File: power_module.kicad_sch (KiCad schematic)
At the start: 3 parts, among them J2 OUTPUT, J3 I2C_BREAKOUT, SW1 ON_OFF

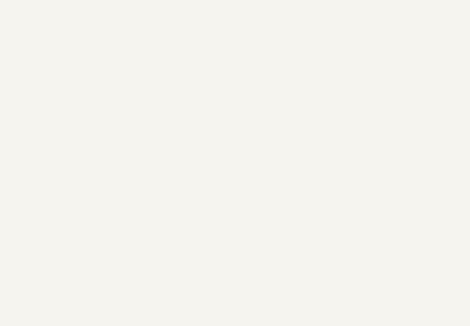
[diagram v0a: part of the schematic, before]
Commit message: add Schematic_Metadata singleton (META1) with mcp_constraint_version=2
First use of the singleton convention from KiCAD-MCP-Server #230.
META1 is a DNP symbol (in_bom no, on_board no) carrying the
project's MCP metadata as properties readable from eeschema's
symbol-properties dialog. Open the schematic in eeschema, select
META1 (top-left of the sheet), and you'll see the metadata fields
alongside Reference/Value.

Currently just the version marker; per-pad Pin_Spring_Class tags
on bypass caps (C29/C30/C3/C4) are next per the workflow doc.

Co-Authored-By: Claude Opus 4.7 <noreply@anthropic.com>
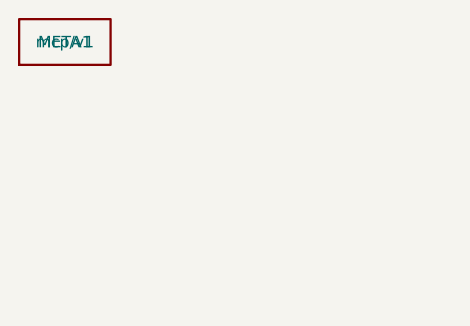
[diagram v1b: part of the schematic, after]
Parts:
- added META1: mcp/v1, symbol mcp_meta:Schematic_Metadata
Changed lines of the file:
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@@
 	)
 	(embedded_fonts no)
+	(symbol
+		(lib_id "mcp_meta:Schematic_Metadata")
+		(at 12.7 12.7 0)
+		(unit 1)
+		(exclude_from_sim yes)
+		(in_bom no)
+		(on_board no)
+		(dnp no)
+		(property "Reference" "META1"
+			(at 12.7 12.7 0)
+			(effects
+				(font
+					(size 1.27 1.27)
+				)
+			)
+		)
+		(property "Value" "mcp/v1"
+			(at 12.7 12.7 0)
+			(effects
+				(font
+					(size 1.27 1.27)
+				)
+			)
+		)
+		(property "Footprint" ""
+			(at 12.7 12.7 0)
+			(effects
+				(font
+					(size 1.27 1.27)
+				)
+				(hide yes)
+			)
+		)
+		(property "Datasheet" ""
+			(at 12.7 12.7 0)
+			(effects
+				(font
+					(size 1.27 1.27)
+				)
+				(hide yes)
+			)
+		)
+		(property "Description" "Project-wide MCP metadata (singleton)."
+			(at 12.7 12.7 0)
+			(effects
+				(font
+					(size 1.27 1.27)
+				)
+				(hide yes)
+			)
+		)
+		(property "Schematic_Metadata_Marker" "mcp/v1"
+			(at 12.7 12.7 0)
+			(effects
+				(font
+					(size 1.27 1.27)
+				)
+				(hide yes)
+			)
+		)
+		(property "mcp_constraint_version" "2"
+			(at 12.7 12.7 0)
+			(effects
+				(font
+					(size 1.27 1.27)
+				)
+				(hide yes)
+			)
+		)
+		(instances
+			(project "power_module"
+				(path "/b0f4a1bd-53e2-4ffd-a882-09b61a25e2e6"
+					(reference "META1")
+					(unit 1)
+				)
+			)
+		)
+	)
 )

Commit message: charger: per-target spring annotations + selective autoplace of U3 group
Annotate U3's decoupling/bulk/bootstrap caps with per-target
Pin_Spring_Class ({"U3.N": "DECOUPLING"}) so each is pulled onto the
specific pin it serves rather than everything on its rail; status LED
D1 weakly tethered (INTER_GROUP). Classify USB_VBUS as INTER_GROUP in
the META1 spring-class net map (cross-group rail; stops Q2 drifting to
the input side). Selectively relax the charger satellites with U3
anchored and all other groups locked.

Co-Authored-By: Claude Opus 4.7 <noreply@anthropic.com>
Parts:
- META1: mcp_spring_classes (none) -> {"nets": {"USB_VBUS": "INTER_GROUP"}}
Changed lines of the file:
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@@
+			)
+		)
+		(property "mcp_spring_classes" "{\"nets\": {\"USB_VBUS\": \"INTER_GROUP\"}}"
+			(at 12.7 12.7 0)
+			(effects
+				(font
+					(size 1.27 1.27)
+				)
+				(hide yes)
 			)
 		)
